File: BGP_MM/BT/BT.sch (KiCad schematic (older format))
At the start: 36 parts, among them J1 Conn_01x02_Male, J2 Conn_01x02_Male, J3 Conn_01x04_Male, J4 Conn_01x04_Male, Q1 MMBF5457, U1 MC33178

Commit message: MM Connector Verification
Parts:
- RV1: symbol POT -> POT-RESCUE-BT
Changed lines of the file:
@@
 EESchema Schematic File Version 2
+LIBS:BT-rescue
 LIBS:power
 LIBS:device
 LIBS:switches
 LIBS:relays
-LIBS:motors
 LIBS:transistors
 LIBS:conn
@@
 $EndComp
 $Comp
-L POT RV1
+L POT-RESCUE-BT RV1
 U 1 1 5B089278
 P 5600 4250

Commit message: MM Switches and BOM
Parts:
- C12: value 100p -> 120p
- C4: footprint Capacitors_SMD:C_0805 -> Capacitors_SMD:C_0603
- R12, R14: value 22k -> 20k
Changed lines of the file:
@@
 F 0 "C4" H 5260 4320 50  0000 L CNN
 F 1 "1.8n" H 5260 4170 50  0000 L CNN
-F 2 "Capacitors_SMD:C_0805" H 5250 4250 50  0001 C CNN
+F 2 "Capacitors_SMD:C_0603" H 5250 4250 50  0001 C CNN
 F 3 "" H 5250 4250 50  0001 C CNN
 	1    5250 4250
@@
 P 6900 3550
 F 0 "R12" H 6930 3570 50  0000 L CNN
-F 1 "22k" H 6930 3510 50  0000 L CNN
+F 1 "20k" H 6930 3510 50  0000 L CNN
 F 2 "Resistors_SMD:R_0603" H 6900 3550 50  0001 C CNN
 F 3 "" H 6900 3550 50  0001 C CNN
@@
 P 7350 4000
 F 0 "R14" H 7380 4020 50  0000 L CNN
-F 1 "22k" H 7380 3960 50  0000 L CNN
+F 1 "20k" H 7380 3960 50  0000 L CNN
 F 2 "Resistors_SMD:R_0603" H 7350 4000 50  0001 C CNN
 F 3 "" H 7350 4000 50  0001 C CNN
@@
 P 7350 4300
 F 0 "C12" H 7360 4370 50  0000 L CNN
-F 1 "100p" H 7360 4220 50  0000 L CNN
+F 1 "120p" H 7360 4220 50  0000 L CNN
 F 2 "Capacitors_SMD:C_0603" H 7350 4300 50  0001 C CNN
 F 3 "" H 7350 4300 50  0001 C CNN

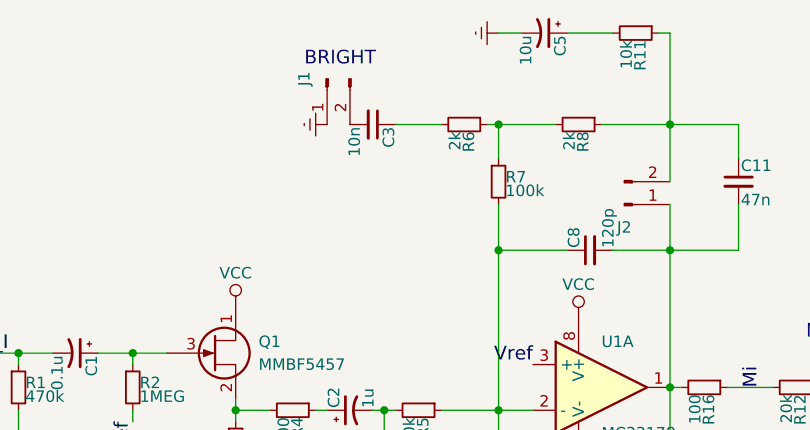
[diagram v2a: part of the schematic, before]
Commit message: BT Bright Cap/Res changed
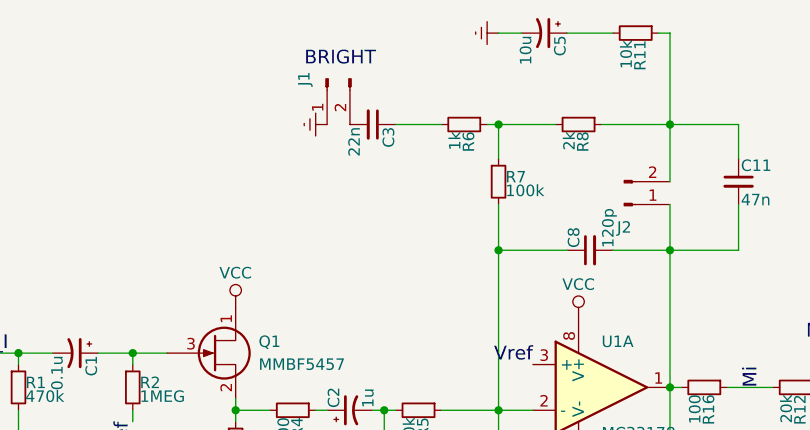
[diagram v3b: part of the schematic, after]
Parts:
- C3: value 10n -> 22n; footprint Capacitors_SMD:C_0805 -> Capacitors_SMD:C_1206
- R6: value 2k -> 1k
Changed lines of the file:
@@
 LIBS:switches
 LIBS:relays
+LIBS:motors
 LIBS:transistors
 LIBS:conn
@@
 P 5450 2400
 F 0 "R6" H 5480 2420 50  0000 L CNN
-F 1 "2k" H 5480 2360 50  0000 L CNN
+F 1 "1k" H 5480 2360 50  0000 L CNN
 F 2 "Resistors_SMD:R_0603" H 5450 2400 50  0001 C CNN
 F 3 "" H 5450 2400 50  0001 C CNN
@@
 P 5050 2400
 F 0 "C3" H 5060 2470 50  0000 L CNN
-F 1 "10n" H 5060 2320 50  0000 L CNN
-F 2 "Capacitors_SMD:C_0805" H 5050 2400 50  0001 C CNN
+F 1 "22n" H 5060 2320 50  0000 L CNN
+F 2 "Capacitors_SMD:C_1206" H 5050 2400 50  0001 C CNN
 F 3 "" H 5050 2400 50  0001 C CNN
 	1    5050 2400

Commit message: MM Refactoring
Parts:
- removed C1: 0.1u, Capacitors_SMD:C_0805, symbol CP1_Small
- removed C13: 1u, Capacitors_SMD:C_0805, symbol CP1_Small
- removed J1: Conn_01x02_Male, Connectors_JST:JST_PH_B2B-PH-K_02x2.00mm_Straight, symbol Conn_01x02_Male
- removed J4: Conn_01x04_Male, Connectors_JST:JST_PH_B4B-PH-K_04x2.00mm_Straight, symbol Conn_01x04_Male
- removed Q1: MMBF5457, TO_SOT_Packages_SMD:SOT-23, symbol Q_NJFET_DSG
- removed R1: 470k, Resistors_SMD:R_0603, symbol R_Small
- removed R13: 200k, Resistors_SMD:R_0603, symbol R_Small
- removed R15: 1k, Resistors_SMD:R_0603, symbol R_Small
- removed R2: 1MEG, Resistors_SMD:R_0603, symbol R_Small
- removed R3: 20k, Resistors_SMD:R_0603, symbol R_Small
- removed R4: 100, Resistors_SMD:R_0603, symbol R_Small
- added C11: 10u, Capacitors_SMD:C_0805, symbol CP1_Small
- added J3: Conn_01x02_Male, Connectors_JST:JST_PH_B2B-PH-K_02x2.00mm_Straight, symbol Conn_01x02_Male
- C2: renamed from C12; footprint Capacitors_SMD:C_0603 -> Capacitors_SMD:C_0603_HandSoldering
- C4: footprint Capacitors_SMD:C_0603 -> Capacitors_SMD:C_0805
- C6, C9: value 47u -> 10u; footprint Capacitors_SMD:C_1206 -> Capacitors_SMD:C_0805
- C7, C8: footprint Capacitors_SMD:C_0603 -> Capacitors_SMD:C_0603_HandSoldering
- R1: renamed from R12; value 20k -> 470k; footprint Resistors_SMD:R_0603 -> Capacitors_SMD:C_0603_HandSoldering
- R10: renamed from R16; value 100 -> 1k; footprint Resistors_SMD:R_0603 -> Capacitors_SMD:C_0603_HandSoldering
- R2: renamed from R14; value 20k -> 470k; footprint Resistors_SMD:R_0603 -> Capacitors_SMD:C_0603_HandSoldering
- R3: renamed from R5; footprint Resistors_SMD:R_0603 -> Capacitors_SMD:C_0603_HandSoldering
- R4: renamed from R6; footprint Resistors_SMD:R_0603 -> Capacitors_SMD:C_0603_HandSoldering
- R5: renamed from R7; footprint Resistors_SMD:R_0603 -> Capacitors_SMD:C_0603_HandSoldering
- R6: renamed from R8; footprint Resistors_SMD:R_0603 -> Capacitors_SMD:C_0603_HandSoldering
- R7: renamed from R9; value 20k -> 100k; footprint Resistors_SMD:R_0603 -> Capacitors_SMD:C_0603_HandSoldering
- R8: renamed from R10; value 20k -> 100k; footprint Resistors_SMD:R_0603 -> Capacitors_SMD:C_0603_HandSoldering
- R9: renamed from R11; footprint Resistors_SMD:R_0603 -> Capacitors_SMD:C_0603_HandSoldering
- renumbered C2 to C1, C11 to C10, J2 to J1, J3 to J2
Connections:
- net Earth: now also J3.1 (Pin_1)
- net SIG_I: now also C1.2
- net VCC: now also J3.2 (Pin_2); no longer J2.3 (Pin_3)
- net Vref: now also U1.3 (+), U1.5 (+); no longer U1.3 (+)
- net at C1.1: now also R1.2
- net at C4.1, R3.2: now also C2.1, R2.1, U1.1; no longer C1.2
- net at C8.1, R3.1, R5.2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: now also U1.6 (-); no longer U1.2 (-)
- net at C10.2, C7.2, C8.2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: now also U1.7; no longer U1.1
- net at C2.2, R1.1, R2.2: now also U1.2 (-); no longer U1.6 (-)
- net BR_O: now reaches J2.1 (Pin_1)
- net BR_O: now also C3.2
- net Mi: no longer names the net of R10.1
- net Mi: now also C11.1; no longer R1.2
- removed net Mo: C2.1, R2.1, U1.7
- removed net Mr: U1.5 (+)
- new net: C11.2, J2.3 (Pin_3)
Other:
- note added: "BASS\nA250K"
- note added: "TO SEL"
- note added: "TREBLE\nC1M"
- note removed: "TO MID"
- moved on the sheet: C1, C2, J2, R1, R2

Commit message: MM Refactoring
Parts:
- removed J2: Conn_01x04_Male, Connectors_JST:JST_PH_B4B-PH-K_04x2.00mm_Straight, symbol Conn_01x04_Male
- removed J3: Conn_01x02_Male, Connectors_JST:JST_PH_B2B-PH-K_02x2.00mm_Straight, symbol Conn_01x02_Male
- added J2: Conn_01x05_Male, Pin_Headers:Pin_Header_Straight_1x05_Pitch2.54mm, symbol Conn_01x05_Male
- C1: value 1u -> 0.1u
- C2: value 120p -> 10p
- C3: value 22n -> 2.7n; footprint Capacitors_SMD:C_1206 -> Capacitors_SMD:C_0805
- C6, C9: footprint Capacitors_SMD:C_0805 -> Capacitors_SMD:C_1206
- R10: value 1k -> 100
- R4: value 1k -> 4.7k
- R6: value 2k -> 10k
- U1: value MC33178 -> TS512A
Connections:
- net BR_O: now also J2.2 (Pin_2)
- net Earth: now also J2.5 (Pin_5)
- net SIG_I: now also J2.3 (Pin_3)
- net VCC: now also J2.1 (Pin_1)
- net at C11.2: now also J2.4 (Pin_4)
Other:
- note removed: "TO SEL"
- note removed: "TO VOL"
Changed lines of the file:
@@
 LIBS:switches
 LIBS:relays
+LIBS:motors
 LIBS:transistors
 LIBS:conn
@@
 P 3900 3750
 F 0 "C1" H 3910 3820 50  0000 L CNN
-F 1 "1u" H 3910 3670 50  0000 L CNN
+F 1 "0.1u" H 3910 3670 50  0000 L CNN
 F 2 "Capacitors_SMD:C_0805" H 3900 3750 50  0001 C CNN
 F 3 "" H 3900 3750 50  0001 C CNN
@@
 P 6050 3550
 F 0 "U1" H 6050 3750 50  0000 L CNN
-F 1 "MC33178" H 6050 3350 50  0000 L CNN
+F 1 "TS512A" H 6050 3350 50  0000 L CNN
 F 2 "SMD_Packages:SOIC-8-N" H 6050 3550 50  0001 C CNN
 F 3 "" H 6050 3550 50  0001 C CNN
@@
 P 4700 3650
 F 0 "U1" H 4700 3850 50  0000 L CNN
-F 1 "MC33178" H 4700 3450 50  0000 L CNN
+F 1 "TS512A" H 4700 3450 50  0000 L CNN
 F 2 "SMD_Packages:SOIC-8-N" H 4700 3650 50  0001 C CNN
 F 3 "" H 4700 3650 50  0001 C CNN
@@
 $EndComp
 $Comp
-L C_Small C2
-U 1 1 5AFF6F5E
-P 4600 4550
-F 0 "C2" H 4610 4620 50  0000 L CNN
-F 1 "120p" H 4610 4470 50  0000 L CNN
-F 2 "Capacitors_SMD:C_0603_HandSoldering" H 4600 4550 50  0001 C CNN
-F 3 "" H 4600 4550 50  0001 C CNN
-	1    4600 4550
-	0    1    1    0
-$EndComp
-$Comp
 L R_Small R7
 U 1 1 5AFF7506
@@
 F 0 "C9" H 6410 5070 50  0000 L CNN
 F 1 "10u" H 6410 4920 50  0000 L CNN
-F 2 "Capacitors_SMD:C_0805" H 6400 5000 50  0001 C CNN
+F 2 "Capacitors_SMD:C_1206" H 6400 5000 50  0001 C CNN
 F 3 "" H 6400 5000 50  0001 C CNN
 	1    6400 5000
@@
 F 0 "C6" H 5810 5070 50  0000 L CNN
 F 1 "10u" H 5810 4920 50  0000 L CNN
-F 2 "Capacitors_SMD:C_0805" H 5800 5000 50  0001 C CNN
+F 2 "Capacitors_SMD:C_1206" H 5800 5000 50  0001 C CNN
 F 3 "" H 5800 5000 50  0001 C CNN
 	1    5800 5000
@@
 SIG_I
 $Comp
-L Conn_01x04_Male J2
-U 1 1 5B03D2CD
-P 7300 3450
-F 0 "J2" H 7300 3650 50  0000 C CNN
-F 1 "Conn_01x04_Male" H 7300 3150 50  0001 C CNN
-F 2 "Connectors_JST:JST_PH_B4B-PH-K_04x2.00mm_Straight" H 7300 3450 50  0001 C CNN
-F 3 "" H 7300 3450 50  0001 C CNN
-	1    7300 3450
-	-1   0    0    -1
-$EndComp
-$Comp
 L C_Small C10
 U 1 1 5B03D8BB
@@
 P 5450 2400
 F 0 "R4" H 5480 2420 50  0000 L CNN
-F 1 "1k" H 5480 2360 50  0000 L CNN
+F 1 "4.7k" H 5480 2360 50  0000 L CNN
 F 2 "Capacitors_SMD:C_0603_HandSoldering" H 5450 2400 50  0001 C CNN
 F 3 "" H 5450 2400 50  0001 C CNN
@@
 P 5950 2400
 F 0 "R6" H 5980 2420 50  0000 L CNN
-F 1 "2k" H 5980 2360 50  0000 L CNN
+F 1 "10k" H 5980 2360 50  0000 L CNN
 F 2 "Capacitors_SMD:C_0603_HandSoldering" H 5950 2400 50  0001 C CNN
 F 3 "" H 5950 2400 50  0001 C CNN
@@
 	0    1    1    0
 $EndComp
-Text Notes 7350 3350 0    60   ~ 0
-TO SEL
 Text Notes 4700 2250 0    60   ~ 0
 BRIGHT
@@
 P 5050 2400
 F 0 "C3" H 5060 2470 50  0000 L CNN
-F 1 "22n" H 5060 2320 50  0000 L CNN
-F 2 "Capacitors_SMD:C_1206" H 5050 2400 50  0001 C CNN
+F 1 "2.7n" H 5060 2320 50  0000 L CNN
+F 2 "Capacitors_SMD:C_0805" H 5050 2400 50  0001 C CNN
 F 3 "" H 5050 2400 50  0001 C CNN
 	1    5050 2400
@@
 P 6500 3550
 F 0 "R10" H 6530 3570 50  0000 L CNN
-F 1 "1k" H 6530 3510 50  0000 L CNN
+F 1 "100" H 6530 3510 50  0000 L CNN
 F 2 "Capacitors_SMD:C_0603_HandSoldering" H 6500 3550 50  0001 C CNN
 F 3 "" H 6500 3550 50  0001 C CNN
@@
 Text Label 7100 3450 2    60   ~ 0
 SIG_I
-$Comp
-L Earth #PWR08
-U 1 1 5B19F59A
-P 7100 3650
-F 0 "#PWR08" H 7100 3400 50  0001 C CNN
-F 1 "Earth" H 7100 3500 50  0001 C CNN
-F 2 "" H 7100 3650 50  0001 C CNN
-F 3 "" H 7100 3650 50  0001 C CNN
-	1    7100 3650
-	0    1    1    0
-$EndComp
 Text Label 4950 2400 2    60   ~ 0
 BR_O
@@
 TREBLE\nC1M
 $Comp
-L Conn_01x02_Male J3
-U 1 1 5B1A1899
-P 7300 4050
-F 0 "J3" H 7300 3850 50  0000 C CNN
-F 1 "Conn_01x02_Male" H 7300 3850 50  0001 C CNN
-F 2 "Connectors_JST:JST_PH_B2B-PH-K_02x2.00mm_Straight" H 7300 4050 50  0001 C CNN
-F 3 "" H 7300 4050 50  0001 C CNN
-	1    7300 4050
-	-1   0    0    1
-$EndComp
-$Comp
-L VCC #PWR09
+L VCC #PWR08
 U 1 1 5B1A1988
-P 7100 3950
-F 0 "#PWR09" H 7100 3800 50  0001 C CNN
-F 1 "VCC" H 7100 4100 50  0000 C CNN
-F 2 "" H 7100 3950 50  0001 C CNN
-F 3 "" H 7100 3950 50  0001 C CNN
-	1    7100 3950
-	1    0    0    -1
-$EndComp
-$Comp
-L Earth #PWR010
+P 7100 3250
+F 0 "#PWR08" H 7100 3100 50  0001 C CNN
+F 1 "VCC" H 7100 3400 50  0000 C CNN
+F 2 "" H 7100 3250 50  0001 C CNN
+F 3 "" H 7100 3250 50  0001 C CNN
+	1    7100 3250
+	1    0    0    -1
+$EndComp
+$Comp
+L Earth #PWR09
 U 1 1 5B1A19E7
-P 7100 4050
-F 0 "#PWR010" H 7100 3800 50  0001 C CNN
-F 1 "Earth" H 7100 3900 50  0001 C CNN
-F 2 "" H 7100 4050 50  0001 C CNN
-F 3 "" H 7100 4050 50  0001 C CNN
-	1    7100 4050
-	1    0    0    -1
-$EndComp
-Text Notes 7350 3950 0    60   ~ 0
-TO VOL
+P 7100 3650
+F 0 "#PWR09" H 7100 3400 50  0001 C CNN
+F 1 "Earth" H 7100 3500 50  0001 C CNN
+F 2 "" H 7100 3650 50  0001 C CNN
+F 3 "" H 7100 3650 50  0001 C CNN
+	1    7100 3650
+	1    0    0    -1
+$EndComp
 Wire Wire Line
 	7100 3550 6850 3550
+$Comp
+L Conn_01x05_Male J2
+U 1 1 5B1AEDDB
+P 7300 3450
+F 0 "J2" H 7300 3750 50  0000 C CNN
+F 1 "Conn_01x05_Male" H 7300 3150 50  0000 C CNN
+F 2 "Pin_Headers:Pin_Header_Straight_1x05_Pitch2.54mm" H 7300 3450 50  0001 C CNN
+F 3 "" H 7300 3450 50  0001 C CNN
+	1    7300 3450
+	-1   0    0    -1
+$EndComp
+$Comp
+L C_Small C2
+U 1 1 5AFF6F5E
+P 4600 4550
+F 0 "C2" H 4610 4620 50  0000 L CNN
+F 1 "10p" H 4610 4470 50  0000 L CNN
+F 2 "Capacitors_SMD:C_0603_HandSoldering" H 4600 4550 50  0001 C CNN
+F 3 "" H 4600 4550 50  0001 C CNN
+	1    4600 4550
+	0    1    1    0
+$EndComp
 $EndSCHEMATC

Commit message: MM Gerbers
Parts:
- removed C2: 10p, Capacitors_SMD:C_0603_HandSoldering, symbol C_Small
- removed C5: 10u, Capacitors_SMD:C_0805, symbol CP1_Small
- added C2: 10u, Capacitors_SMD:C_0805, symbol CP1_Small
- added C5: 10p, Capacitors_SMD:C_0603_HandSoldering, symbol C_Small
- added R11: 100, Capacitors_SMD:C_0603_HandSoldering, symbol R_Small
- C10: value 47n -> 2.7n; footprint Capacitors_SMD:C_1206 -> Capacitors_SMD:C_0805
- C4: value 1.8n -> 2.7n
- C7: value 470p -> 100p
- C8: value 120p -> 100p
- J1: footprint Connectors_JST:JST_PH_B2B-PH-K_02x2.00mm_Straight -> Pin_Headers:Pin_Header_Straight_1x02
- R2: value 470k -> 10k
- R3: value 220k -> 180k
- R5: value 100k -> 180k
- R9: value 10k -> 180k
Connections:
- net Earth: now also C2.2
- net at C4.1, R3.2: now also R11.1; no longer R2.1, U1.1
- net at C7.2, C8.2, R10.2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: now also R6.1; no longer C10.2, J1.1 (Pin_1)
- net at J1.2 (Pin_2), R9.1: now also C10.2, R2.1; no longer C10.1, R6.1
- net at R9.2: now also R1.1, U1.2 (-), C5.1
- new net: C10.1, C5.2, J1.1 (Pin_1), R11.2, U1.1
- new net: C2.1, R2.2
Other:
- moved on the sheet: C1, C11, C3, C4, C6, C7, C8, C9, D1, J2, R1, R10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

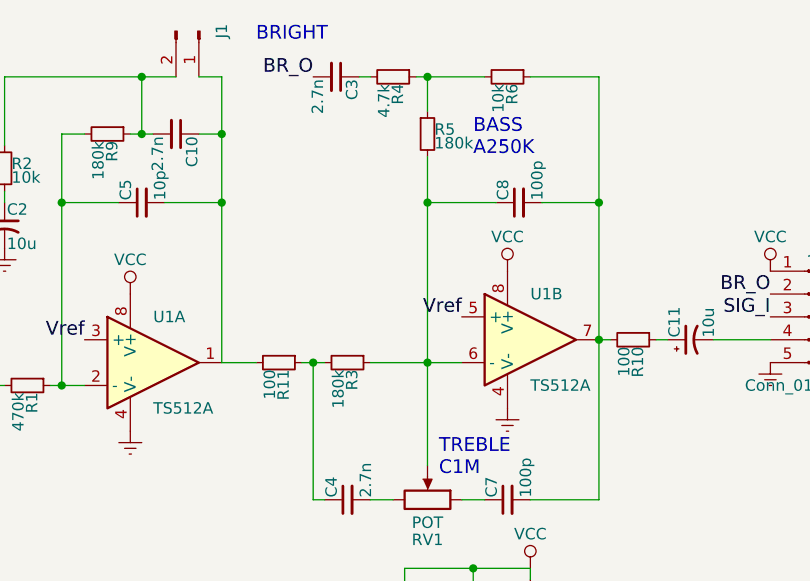
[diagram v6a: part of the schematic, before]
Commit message: Minor BOM changes
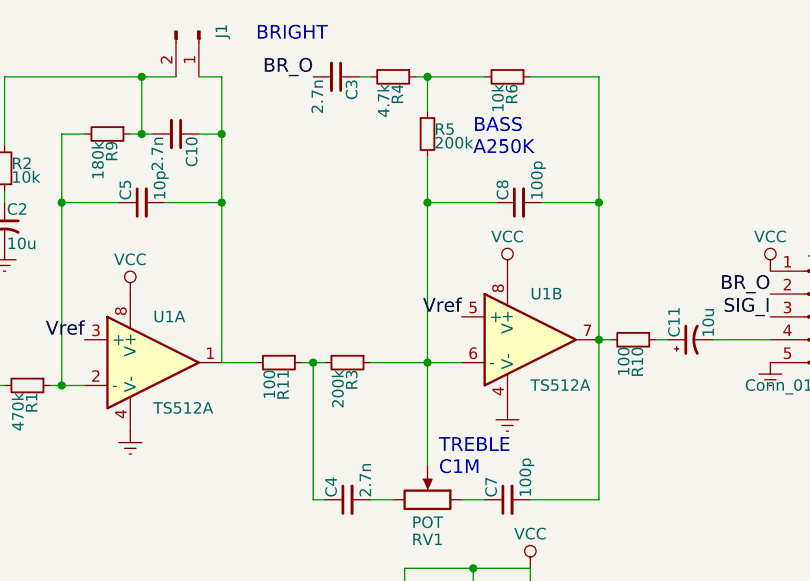
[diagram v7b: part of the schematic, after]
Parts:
- R3, R5: value 180k -> 200k
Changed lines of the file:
@@
 P 6400 3650
 F 0 "R3" H 6430 3670 50  0000 L CNN
-F 1 "180k" H 6430 3610 50  0000 L CNN
+F 1 "200k" H 6430 3610 50  0000 L CNN
 F 2 "Capacitors_SMD:C_0603_HandSoldering" H 6400 3650 50  0001 C CNN
 F 3 "" H 6400 3650 50  0001 C CNN
@@
 P 6750 2650
 F 0 "R5" H 6780 2670 50  0000 L CNN
-F 1 "180k" H 6780 2610 50  0000 L CNN
+F 1 "200k" H 6780 2610 50  0000 L CNN
 F 2 "Capacitors_SMD:C_0603_HandSoldering" H 6750 2650 50  0001 C CNN
 F 3 "" H 6750 2650 50  0001 C CNN
